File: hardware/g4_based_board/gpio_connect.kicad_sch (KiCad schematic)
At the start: 15 parts, among them J14 Screw_Terminal_01x03, Q3 NMOS

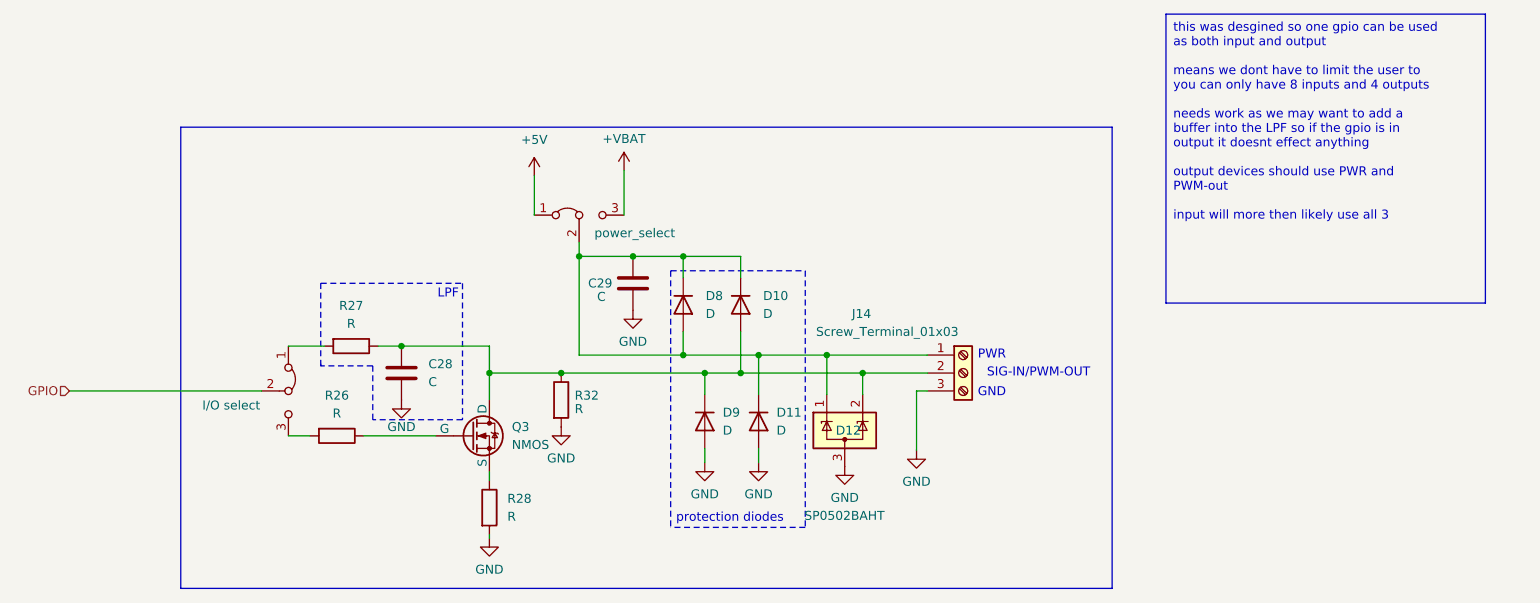
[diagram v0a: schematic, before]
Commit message: now uses hierarchical sheets
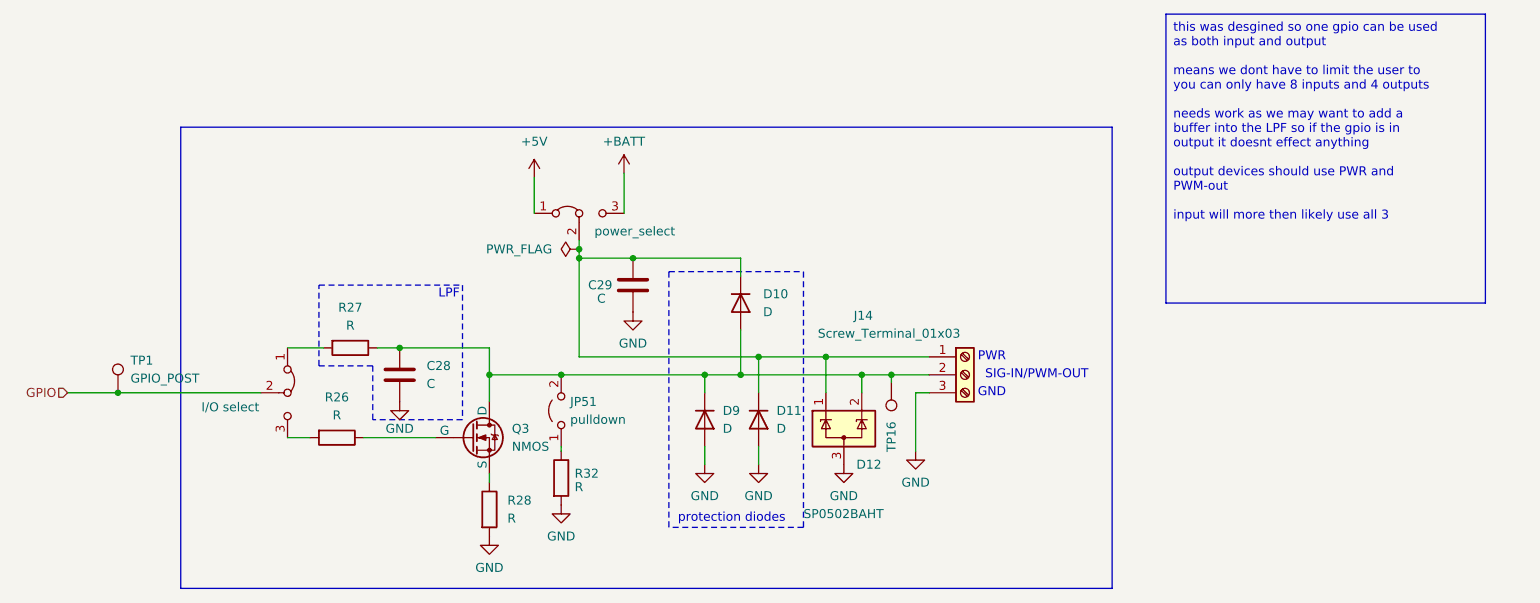
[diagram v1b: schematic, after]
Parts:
- removed D8: D, Diode_SMD:D_0805_2012Metric, symbol Device:D
- added JP51: pulldown, Connector_PinHeader_2.54mm:PinHeader_1x02_P2.54mm_Vertical, symbol Jumper:Jumper_2_Open
- added TP1: GPIO_POST, symbol Connector:TestPoint
- added TP16: GPIO_INPUT_PRE, symbol Connector:TestPoint
- C28, C29: footprint Capacitor_SMD:C_0805_2012Metric -> Capacitor_SMD:C_0603_1608Metric_Pad1.08x0.95mm_HandSolder
- D10, D11, D9: footprint Diode_SMD:D_0805_2012Metric -> Diode_SMD:D_0603_1608Metric
- JP22, JP23: footprint (none) -> Connector_PinHeader_2.54mm:PinHeader_1x03_P2.54mm_Vertical
- Q3: footprint (none) -> Package_TO_SOT_SMD:SOT-23-3
- R26, R27, R28, R32: footprint Resistor_SMD:R_0805_2012Metric -> Resistor_SMD:R_0603_1608Metric_Pad0.98x0.95mm_HandSolder
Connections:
- net GPIO: now also TP1.1
- net at C28.1, D10.2 (A), D12.2 (K)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: now also JP51.2 (B), TP16.1; no longer R32.1
- net +VBAT renamed +BATT
- new net: JP51.1 (A), R32.1
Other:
- moved on the sheet: R32

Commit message: added test point footprint
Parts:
- TP1, TP16: footprint (none) -> TestPoint:TestPoint_Keystone_5019_Minature
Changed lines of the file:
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@@
 			)
 		)
-		(property "Footprint" ""
+		(property "Footprint" "TestPoint:TestPoint_Keystone_5019_Minature"
 			(at 177.546 96.266 0)
 			(effects
@@
 			)
 		)
-		(property "Footprint" ""
+		(property "Footprint" "TestPoint:TestPoint_Keystone_5019_Minature"
 			(at 78.232 97.79 0)
 			(effects

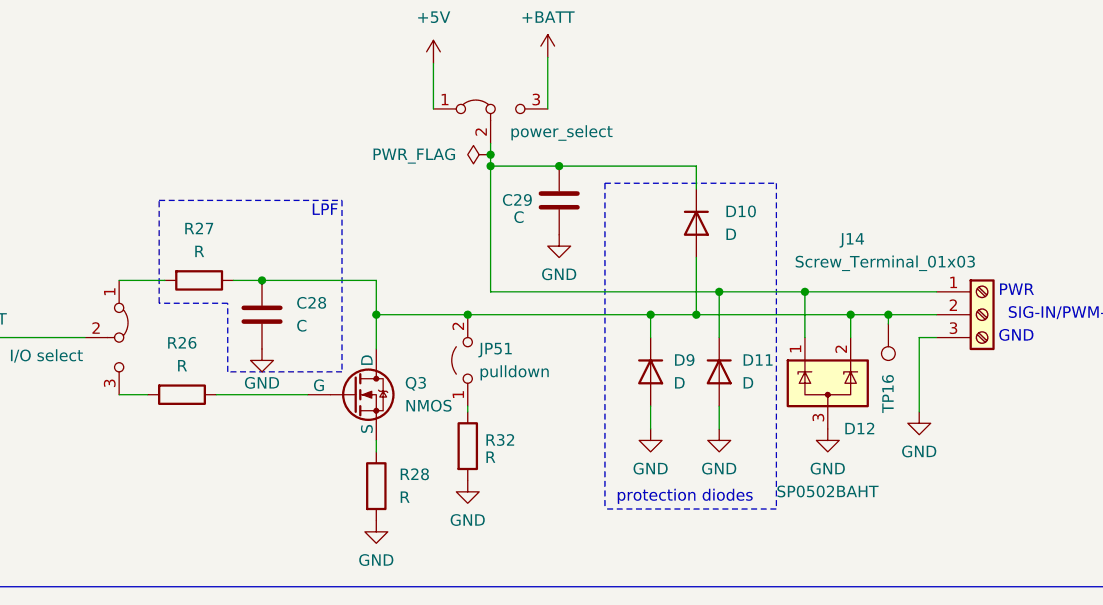
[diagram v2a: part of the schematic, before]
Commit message: removed protection diodes as the tvs diodes are enough
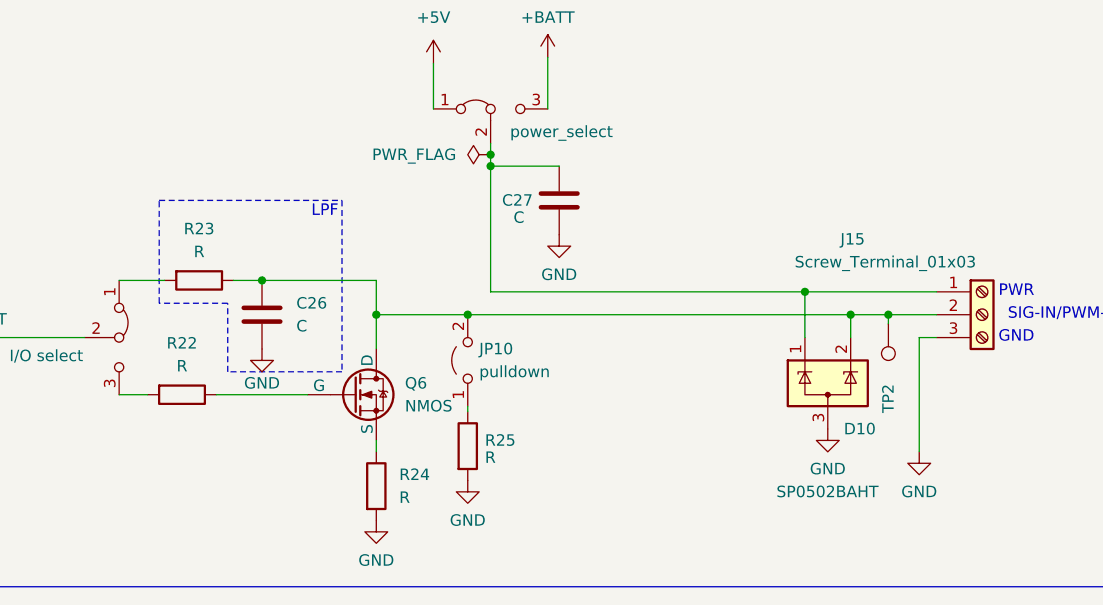
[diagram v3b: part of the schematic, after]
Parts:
- removed D10, D11, D9: D, Diode_SMD:D_0603_1608Metric, symbol Device:D
- renumbered C28 to C26, C29 to C27, D12 to D10, J14 to J15, JP51 to JP10, JP22 to JP25, JP23 to JP27, Q3 to Q6, R26 to R22, R27 to R23, R28 to R24, R32 to R25, TP16 to TP2
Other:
- note removed: "protection diodes"
